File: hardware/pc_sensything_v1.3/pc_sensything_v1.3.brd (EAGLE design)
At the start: 47 x 57 mm, 96 parts, among them IC1 CY8C29666_QFN48, Q1 MBT3904DW1T1, Q2 2.5A/30V, SW2 KMR2, U1 FTS31XS-U, U3 MCP73831, U8 AP2112K-3.3V, Y1 32.768kHz

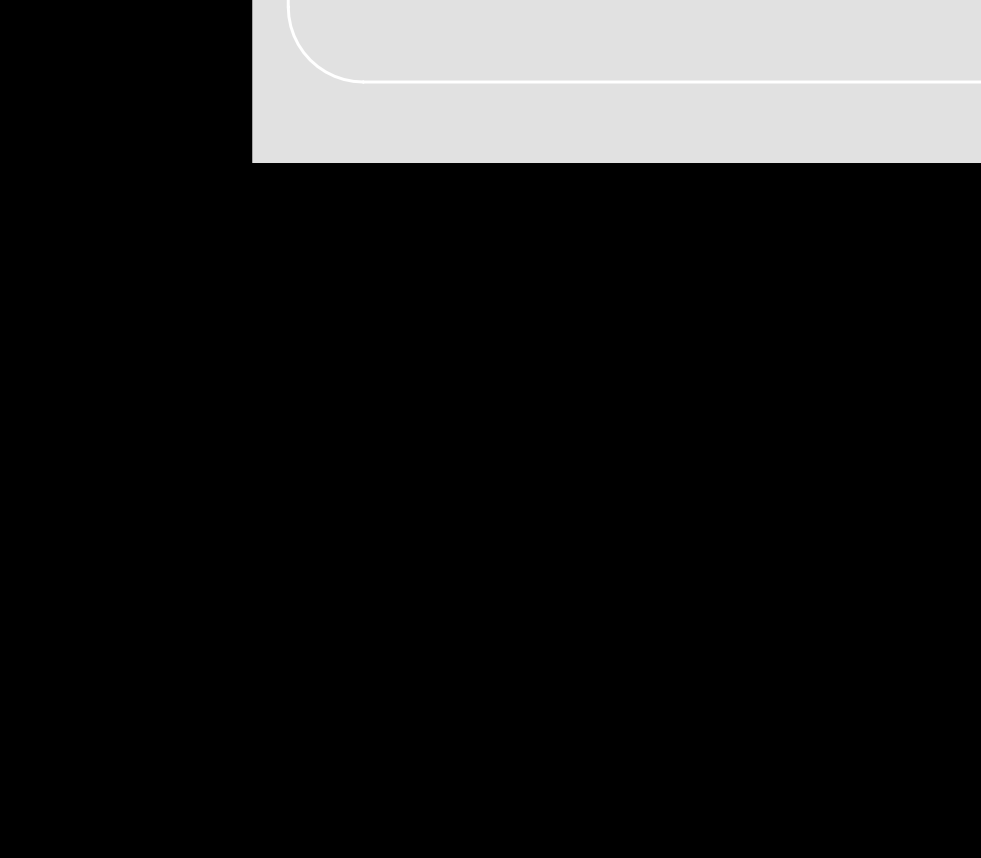
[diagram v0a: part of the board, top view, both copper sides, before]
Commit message: Updated Eagle schematic for v1.3 and PDF
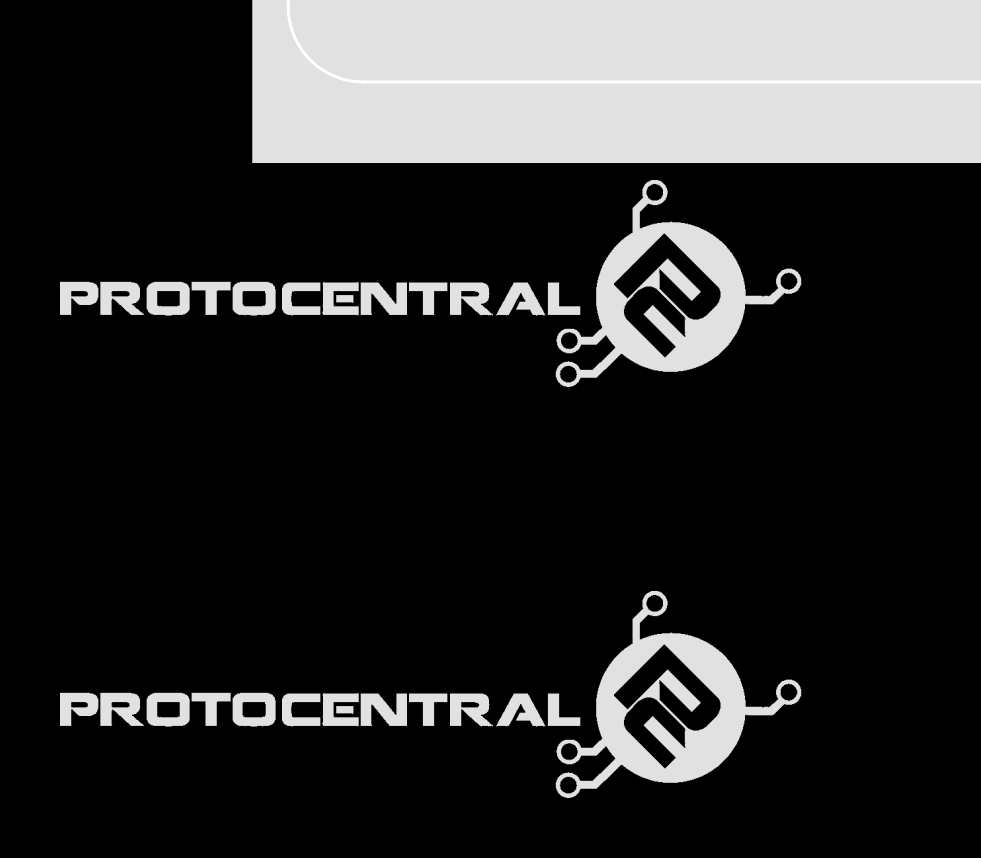
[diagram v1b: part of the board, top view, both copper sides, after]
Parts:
- added U$19, U$21: PROTY_LOGO_WITH_TEXT, circuitects:PROTY_WITH_TEXT
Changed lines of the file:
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@@
 <attribute name="VALUE" x="5.521" y="13.96" size="1.27" layer="27" ratio="10" rot="R90"/>
 </element>
+<element name="U$19" library="circuitects" package="PROTY_WITH_TEXT" value="PROTY_LOGO_WITH_TEXT" x="-7.6" y="-9.8"/>
+<element name="U$21" library="circuitects" package="PROTY_WITH_TEXT" value="PROTY_LOGO_WITH_TEXT" x="-7.6" y="-23.5"/>
 </elements>
 <signals>
